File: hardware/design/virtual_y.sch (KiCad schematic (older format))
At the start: 8 parts

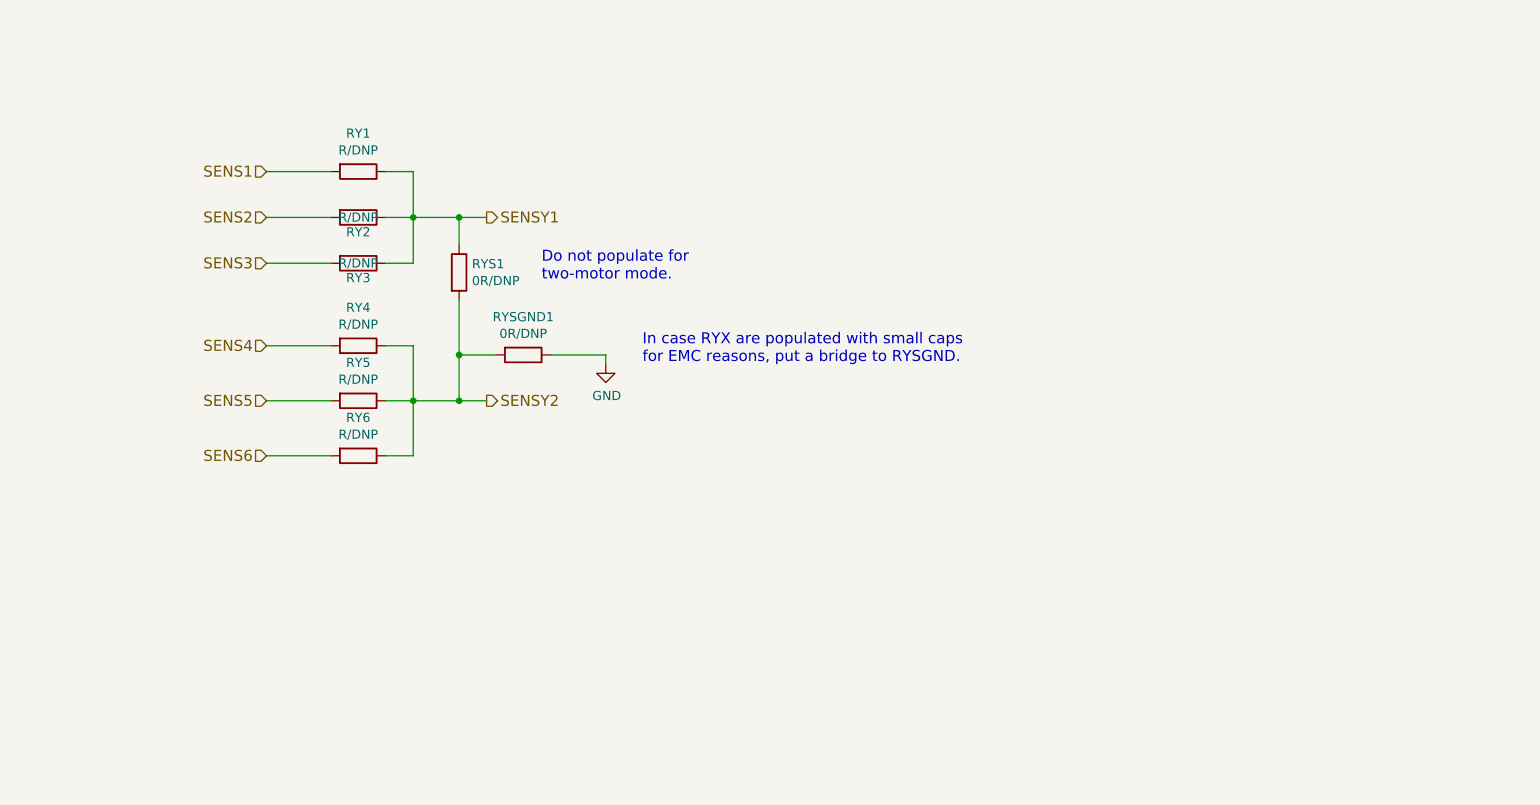
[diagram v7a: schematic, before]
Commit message: Added optional High Frequency AC-coupled voltage sensing port PHFAC
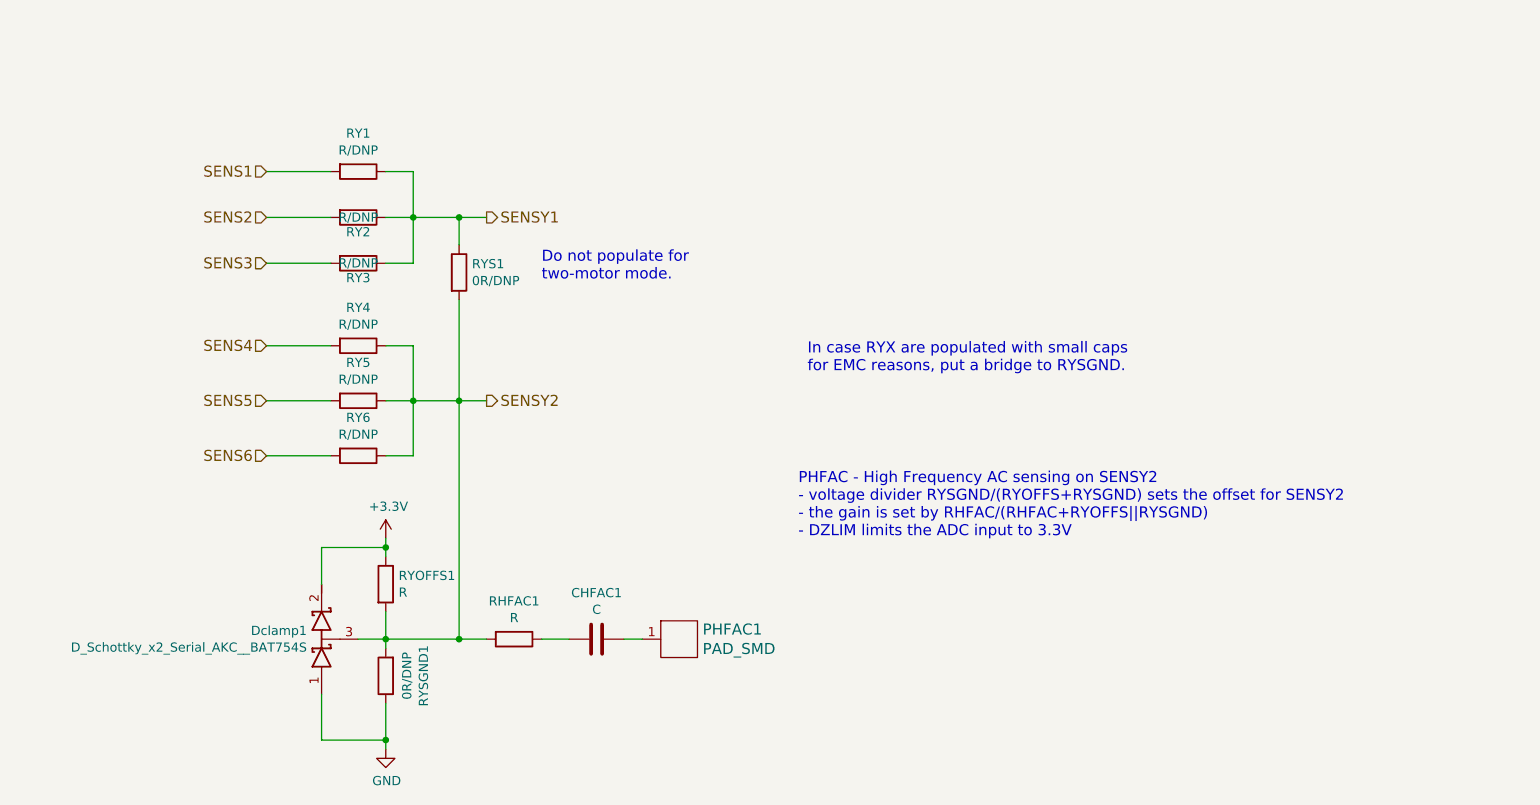
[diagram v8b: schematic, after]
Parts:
- added CHFAC1: C, Capacitors_SMD:C_0603_HandSoldering, symbol C
- added Dclamp1: D_Schottky_x2_Serial_AKC__BAT754S, TO_SOT_Packages_SMD:SOT-23, symbol D_Schottky_x2_Serial_AKC
- added PHFAC1: PAD_SMD, Pads:PAD_SMD_1.2x2.5, symbol PAD_SMD
- added RHFAC1, RYOFFS1: R, Resistors_SMD:R_0603_HandSoldering, symbol R
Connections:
- net GND: now also Dclamp1.1 (A)
- net SENSY2: now also Dclamp1.3 (common), RHFAC1.2, RYOFFS1.2
- new net: CHFAC1.1, PHFAC1.1 (PAD)
- new net: CHFAC1.2, RHFAC1.1
- new net +3V3: Dclamp1.2 (K), RYOFFS1.1
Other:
- note added: "PHFAC - High Frequency AC sensing on SENSY2\n- voltage divider RYSGND/(RYOFFS+RYSGND) sets the offset for SENSY2\n- the gain is set by RHFAC/(RHFAC+RYOFFS||RYSGND)\n- DZLIM limits the ADC input to 3.3V"
- moved on the sheet: RYSGND1
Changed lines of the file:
@@
 	5050 3500 5050 3350
 Wire Wire Line
-	5050 3800 5050 4350
+	5050 3800 5050 5650
 $Comp
 L R RYSGND1
 U 1 1 57935AF7
-P 5400 4100
-F 0 "RYSGND1" V 5193 4100 50  0000 C CNN
-F 1 "0R/DNP" V 5284 4100 50  0000 C CNN
-F 2 "Resistors_SMD:R_0402" V 5330 4100 50  0001 C CNN
-F 3 "" H 5400 4100 50  0000 C CNN
-	1    5400 4100
-	0    1    1    0
+P 4650 5850
+F 0 "RYSGND1" V 4443 5850 50  0000 C CNN
+F 1 "0R/DNP" V 4534 5850 50  0000 C CNN
+F 2 "Resistors_SMD:R_0402" V 4580 5850 50  0001 C CNN
+F 3 "" H 4650 5850 50  0000 C CNN
+	1    4650 5850
+	-1   0    0    1
 $EndComp
-Wire Wire Line
-	5250 4100 5050 4100
-Connection ~ 5050 4100
 $Comp
 L GND #PWR037
 U 1 1 57935C8D
-P 5850 4150
-F 0 "#PWR037" H 5850 3900 50  0001 C CNN
-F 1 "GND" H 5855 3977 50  0000 C CNN
-F 2 "" H 5850 4150 50  0000 C CNN
-F 3 "" H 5850 4150 50  0000 C CNN
-	1    5850 4150
+P 4650 6250
+F 0 "#PWR037" H 4650 6000 50  0001 C CNN
+F 1 "GND" H 4655 6077 50  0000 C CNN
+F 2 "" H 4650 6250 50  0000 C CNN
+F 3 "" H 4650 6250 50  0000 C CNN
+	1    4650 6250
+	1    0    0    -1
+$EndComp
+Text Notes 6950 4200 0    60   ~ 0
+In case RYX are populated with small caps\nfor EMC reasons, put a bridge to RYSGND.
+$Comp
+L PAD_SMD PHFAC1
+U 1 1 579D159A
+P 6250 5650
+F 0 "PHFAC1" H 6378 5703 60  0000 L CNN
+F 1 "PAD_SMD" H 6378 5597 60  0000 L CNN
+F 2 "Pads:PAD_SMD_1.2x2.5" H 6250 5400 60  0001 C CNN
+F 3 "" H 6250 5500 60  0000 C CNN
+	1    6250 5650
+	1    0    0    -1
+$EndComp
+$Comp
+L R RHFAC1
+U 1 1 579D1630
+P 5350 5650
+F 0 "RHFAC1" V 5143 5650 50  0000 C CNN
+F 1 "R" V 5234 5650 50  0000 C CNN
+F 2 "Resistors_SMD:R_0603_HandSoldering" V 5280 5650 50  0001 C CNN
+F 3 "" H 5350 5650 50  0000 C CNN
+	1    5350 5650
+	0    1    1    0
+$EndComp
+$Comp
+L +3.3V #PWR038
+U 1 1 579D18A3
+P 4650 5100
+F 0 "#PWR038" H 4650 4950 50  0001 C CNN
+F 1 "+3.3V" H 4665 5273 50  0000 C CNN
+F 2 "" H 4650 5100 50  0000 C CNN
+F 3 "" H 4650 5100 50  0000 C CNN
+	1    4650 5100
+	1    0    0    -1
+$EndComp
+$Comp
+L C CHFAC1
+U 1 1 579D1951
+P 5800 5650
+F 0 "CHFAC1" V 5548 5650 50  0000 C CNN
+F 1 "C" V 5639 5650 50  0000 C CNN
+F 2 "Capacitors_SMD:C_0603_HandSoldering" H 5838 5500 50  0001 C CNN
+F 3 "" H 5800 5650 50  0000 C CNN
+	1    5800 5650
+	0    1    1    0
+$EndComp
+$Comp
+L R RYOFFS1
+U 1 1 579D1B7A
+P 4650 5350
+F 0 "RYOFFS1" H 4720 5396 50  0000 L CNN
+F 1 "R" H 4720 5305 50  0000 L CNN
+F 2 "Resistors_SMD:R_0603_HandSoldering" V 4580 5350 50  0001 C CNN
+F 3 "" H 4650 5350 50  0000 C CNN
+	1    4650 5350
 	1    0    0    -1
 $EndComp
 Wire Wire Line
-	5550 4100 5850 4100
+	4650 6000 4650 6250
+Connection ~ 4650 6200
 Wire Wire Line
-	5850 4100 5850 4150
-Text Notes 6050 4150 0    60   ~ 0
-In case RYX are populated with small caps\nfor EMC reasons, put a bridge to RYSGND.
+	4650 5500 4650 5700
+Wire Wire Line
+	4500 5650 5200 5650
+Connection ~ 4650 5650
+Connection ~ 5050 5650
+Wire Wire Line
+	5500 5650 5650 5650
+Wire Wire Line
+	5950 5650 6050 5650
+Text Notes 6900 5100 0    60   ~ 0
+PHFAC - High Frequency AC sensing on SENSY2\n- voltage divider RYSGND/(RYOFFS+RYSGND) sets the offset for SENSY2\n- the gain is set by RHFAC/(RHFAC+RYOFFS||RYSGND)\n- DZLIM limits the ADC input to 3.3V
+$Comp
+L D_Schottky_x2_Serial_AKC Dclamp1
+U 1 1 579D5C9B
+P 4300 5650
+F 0 "Dclamp1" V 4346 5730 50  0000 L CNN
+F 1 "D_Schottky_x2_Serial_AKC__BAT754S" V 4255 5730 50  0000 L CNN
+F 2 "TO_SOT_Packages_SMD:SOT-23" H 4300 5650 50  0001 C CNN
+F 3 "" H 4300 5650 50  0000 C CNN
+	1    4300 5650
+	0    -1   -1   0
+$EndComp
+Wire Wire Line
+	4650 5200 4650 5100
+Wire Wire Line
+	4300 5950 4300 6200
+Wire Wire Line
+	4300 6200 4650 6200
+Wire Wire Line
+	4300 5350 4300 5150
+Wire Wire Line
+	4300 5150 4650 5150
+Connection ~ 4650 5150
 $EndSCHEMATC
